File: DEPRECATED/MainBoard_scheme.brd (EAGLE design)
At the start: 80 x 80 mm, 35 parts, among them IC1 7805TV, IC2 VNH3SP30, IC3 VNH3SP30, Q1 SS8050-G, Q2 SS8050-G, SW1 P-B1720, U1 AMS1117-3.3, U2 ESP32-WROOM-32D, U3 CP2102N-A01-GQFN28

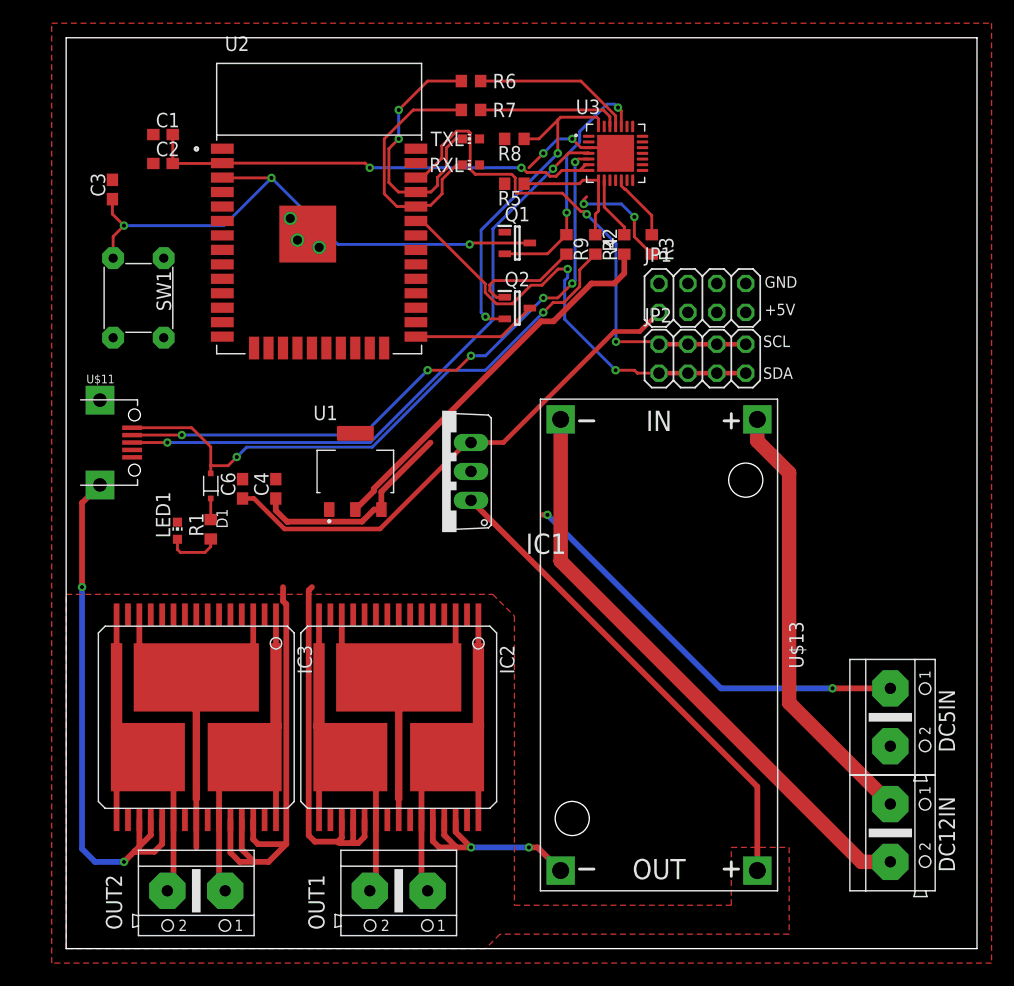
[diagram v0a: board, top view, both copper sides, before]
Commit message: Edit PPMB32-E; prepare PPSB-T for sending gerbers to JLCPCB
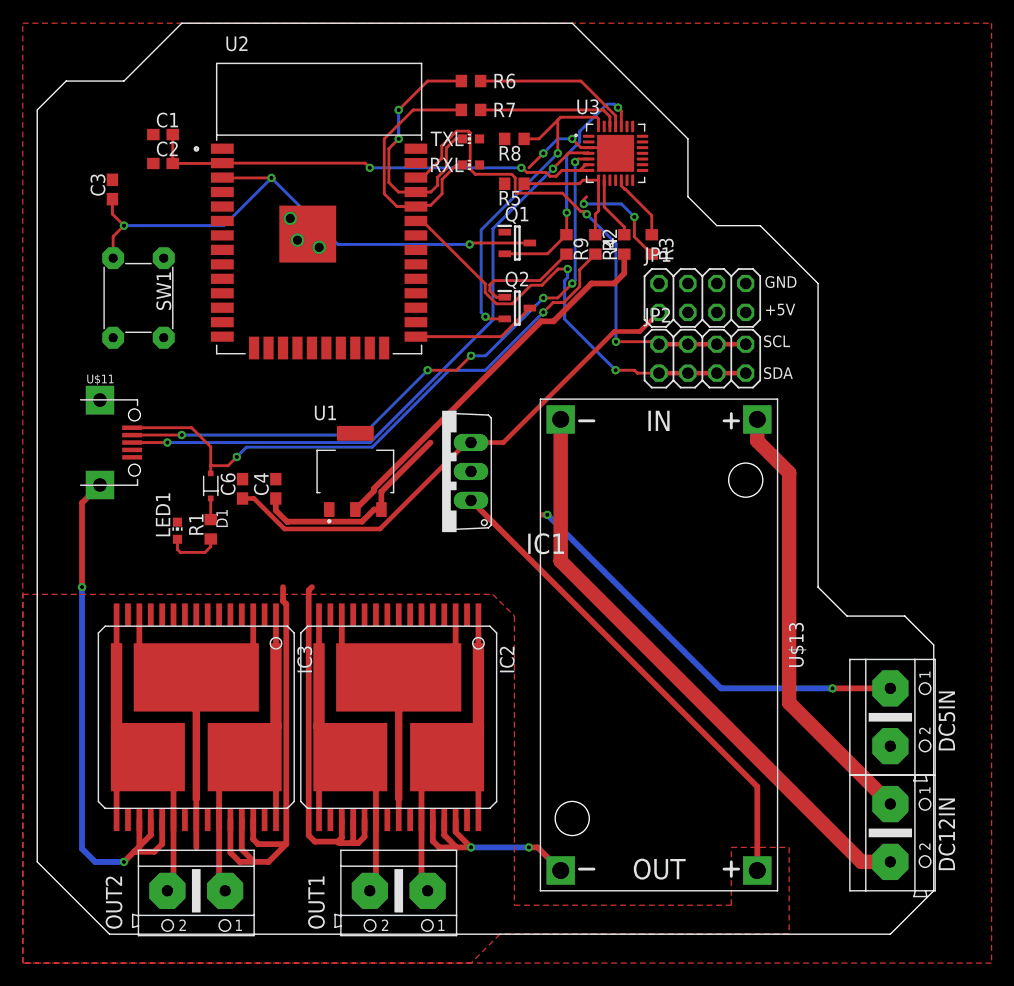
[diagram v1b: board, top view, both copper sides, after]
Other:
- board size 80 x 80 mm -> 78.7 x 80 mm
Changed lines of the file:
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@@
 <board>
 <plain>
-<wire x1="0" y1="0" x2="80" y2="0" width="0" layer="20"/>
-<wire x1="80" y1="0" x2="80" y2="80" width="0" layer="20"/>
-<wire x1="80" y1="80" x2="0" y2="80" width="0" layer="20"/>
-<wire x1="0" y1="80" x2="0" y2="0" width="0" layer="20"/>
 <polygon width="0.254" layer="41">
 <vertex x="11.43" y="80.01"/>
@@
 <text x="61.341" y="55.626" size="1.016" layer="25">+5V</text>
 <text x="61.341" y="58.039" size="1.016" layer="25">GND</text>
+<wire x1="-2.54" y1="7.62" x2="3.81" y2="1.27" width="0.0762" layer="20"/>
+<wire x1="3.81" y1="1.27" x2="72.39" y2="1.27" width="0.0762" layer="20"/>
+<wire x1="72.39" y1="1.27" x2="76.2" y2="5.08" width="0.0762" layer="20"/>
+<wire x1="76.2" y1="5.08" x2="76.2" y2="26.67" width="0.0762" layer="20"/>
+<wire x1="76.2" y1="26.67" x2="73.66" y2="29.21" width="0.0762" layer="20"/>
+<wire x1="73.66" y1="29.21" x2="68.58" y2="29.21" width="0.0762" layer="20"/>
+<wire x1="68.58" y1="29.21" x2="66.04" y2="31.75" width="0.0762" layer="20"/>
+<wire x1="66.04" y1="31.75" x2="66.04" y2="58.42" width="0.0762" layer="20"/>
+<wire x1="66.04" y1="58.42" x2="60.96" y2="63.5" width="0.0762" layer="20"/>
+<wire x1="60.96" y1="63.5" x2="57.15" y2="63.5" width="0.0762" layer="20"/>
+<wire x1="57.15" y1="63.5" x2="54.61" y2="66.04" width="0.0762" layer="20"/>
+<wire x1="54.61" y1="66.04" x2="54.61" y2="71.12" width="0.0762" layer="20"/>
+<wire x1="54.61" y1="71.12" x2="44.45" y2="81.28" width="0.0762" layer="20"/>
+<wire x1="44.45" y1="81.28" x2="10.16" y2="81.28" width="0.0762" layer="20"/>
+<wire x1="10.16" y1="81.28" x2="5.08" y2="76.2" width="0.0762" layer="20"/>
+<wire x1="5.08" y1="76.2" x2="0" y2="76.2" width="0.0762" layer="20"/>
+<wire x1="0" y1="76.2" x2="-2.54" y2="73.66" width="0.0762" layer="20"/>
+<wire x1="-2.54" y1="73.66" x2="-2.54" y2="7.62" width="0.0762" layer="20"/>
 </plain>
 <attributes>
@@
 <contactref element="IC1" pad="2"/>
 <polygon width="0.15" layer="1" rank="6">
-<vertex x="-1.27" y="81.28"/>
+<vertex x="-3.81" y="81.28"/>
 <vertex x="81.28" y="81.28"/>
 <vertex x="81.28" y="-1.27"/>
-<vertex x="-1.27" y="-1.27"/>
+<vertex x="-3.81" y="-1.27"/>
 </polygon>
 <wire x1="45.9" y1="70.35" x2="47.76" y2="70.35" width="0.254" layer="1"/>
@@
 <contactref element="IC3" pad="13"/>
 <polygon width="0.3048" layer="1" rank="2">
-<vertex x="0" y="31.115"/>
+<vertex x="-3.81" y="31.115"/>
 <vertex x="37.465" y="31.115"/>
 <vertex x="39.37" y="29.21"/>
@@
 <vertex x="63.5" y="1.27"/>
 <vertex x="38.1" y="1.27"/>
-<vertex x="36.83" y="0"/>
-<vertex x="0" y="0"/>
+<vertex x="35.56" y="-1.27"/>
+<vertex x="-3.81" y="-1.27"/>
 </polygon>
 <wire x1="11.43" y1="12.32" x2="11.43" y2="8.89" width="0.508" layer="1"/>
